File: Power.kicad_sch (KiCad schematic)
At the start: 8 parts, among them J17 FCR7350B, J18 FCR7350B, J5 1053091102, Q6 AO3401A

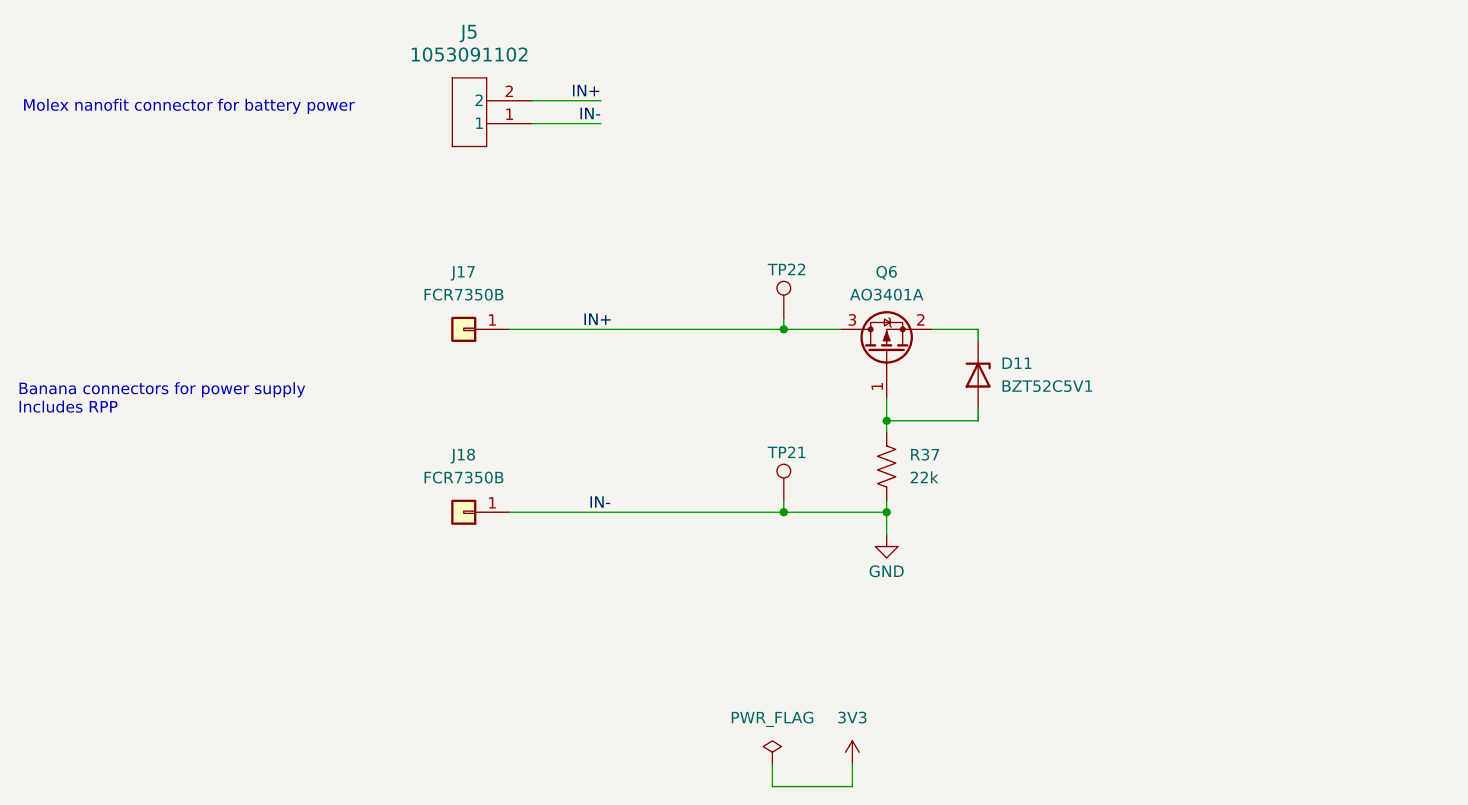
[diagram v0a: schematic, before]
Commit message: Made most capacitors 0402 for mcu sheets, defined board shape and started layout
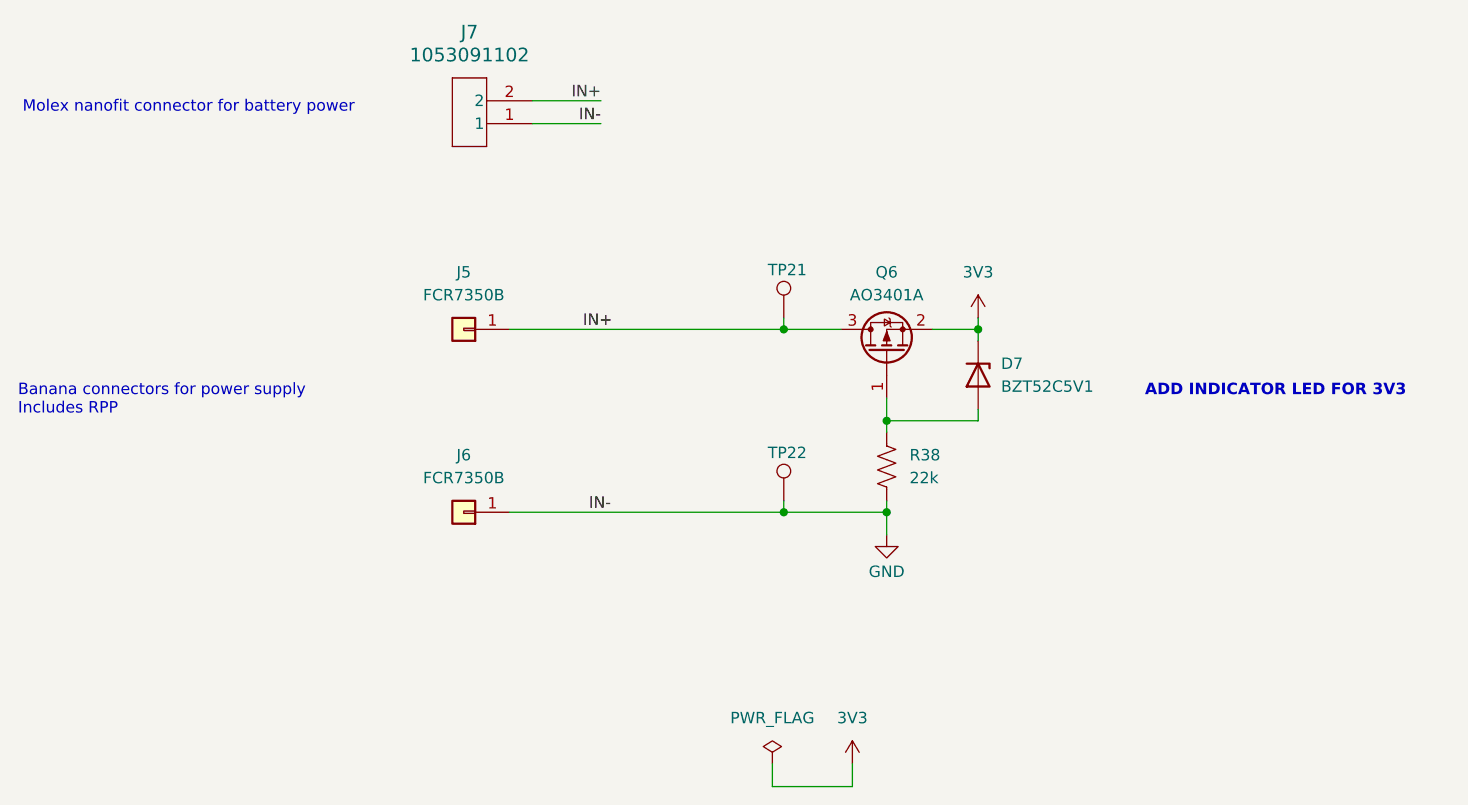
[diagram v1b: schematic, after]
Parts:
- renumbered D11 to D7, J17 to J5, J18 to J6, J5 to J7, R37 to R38, TP22 to TP21, TP21 to TP22
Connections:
- net 3V3: now also D7.1 (K), Q6.2 (S)
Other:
- note added: "ADD INDICATOR LED FOR 3V3"
